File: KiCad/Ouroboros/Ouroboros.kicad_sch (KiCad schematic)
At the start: 0 parts

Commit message: Updating schematic
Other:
- sheet POWER renamed Power
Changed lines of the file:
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@@
 	)
 	(sheet
-		(at 86.36 43.18)
-		(size 12.7 3.81)
+		(at 121.92 34.29)
+		(size 27.94 16.51)
 		(fields_autoplaced yes)
 		(stroke
@@
 			(color 0 0 0 0.0000)
 		)
-		(property "Sheetname" "POWER"
-			(at 86.36 42.4684 0)
+		(property "Sheetname" "Power"
+			(at 121.92 33.5784 0)
 			(effects
 				(font
@@
 		)
 		(property "Sheetfile" "Power.kicad_sch"
-			(at 86.36 47.5746 0)
+			(at 121.92 51.3846 0)
 			(effects
 				(font
@@
 	)
 	(sheet
-		(at 30.48 45.72)
+		(at 29.21 74.93)
 		(size 45.72 36.83)
 		(fields_autoplaced yes)
@@
 		)
 		(property "Sheetname" "Input"
-			(at 30.48 45.0084 0)
+			(at 29.21 74.2184 0)
 			(effects
 				(font
@@
 		)
 		(property "Sheetfile" "input.kicad_sch"
-			(at 30.48 83.1346 0)
+			(at 29.21 112.3446 0)
 			(effects
 				(font
@@
 	)
 	(sheet
-		(at 161.29 53.34)
+		(at 157.48 73.66)
 		(size 64.77 49.53)
 		(fields_autoplaced yes)
@@
 		)
 		(property "Sheetname" "DaisySeed"
-			(at 161.29 52.6284 0)
+			(at 157.48 72.9484 0)
 			(effects
 				(font
@@
 		)
 		(property "Sheetfile" "DaisySeed.kicad_sch"
-			(at 161.29 103.4546 0)
+			(at 157.48 123.7746 0)
 			(effects
 				(font

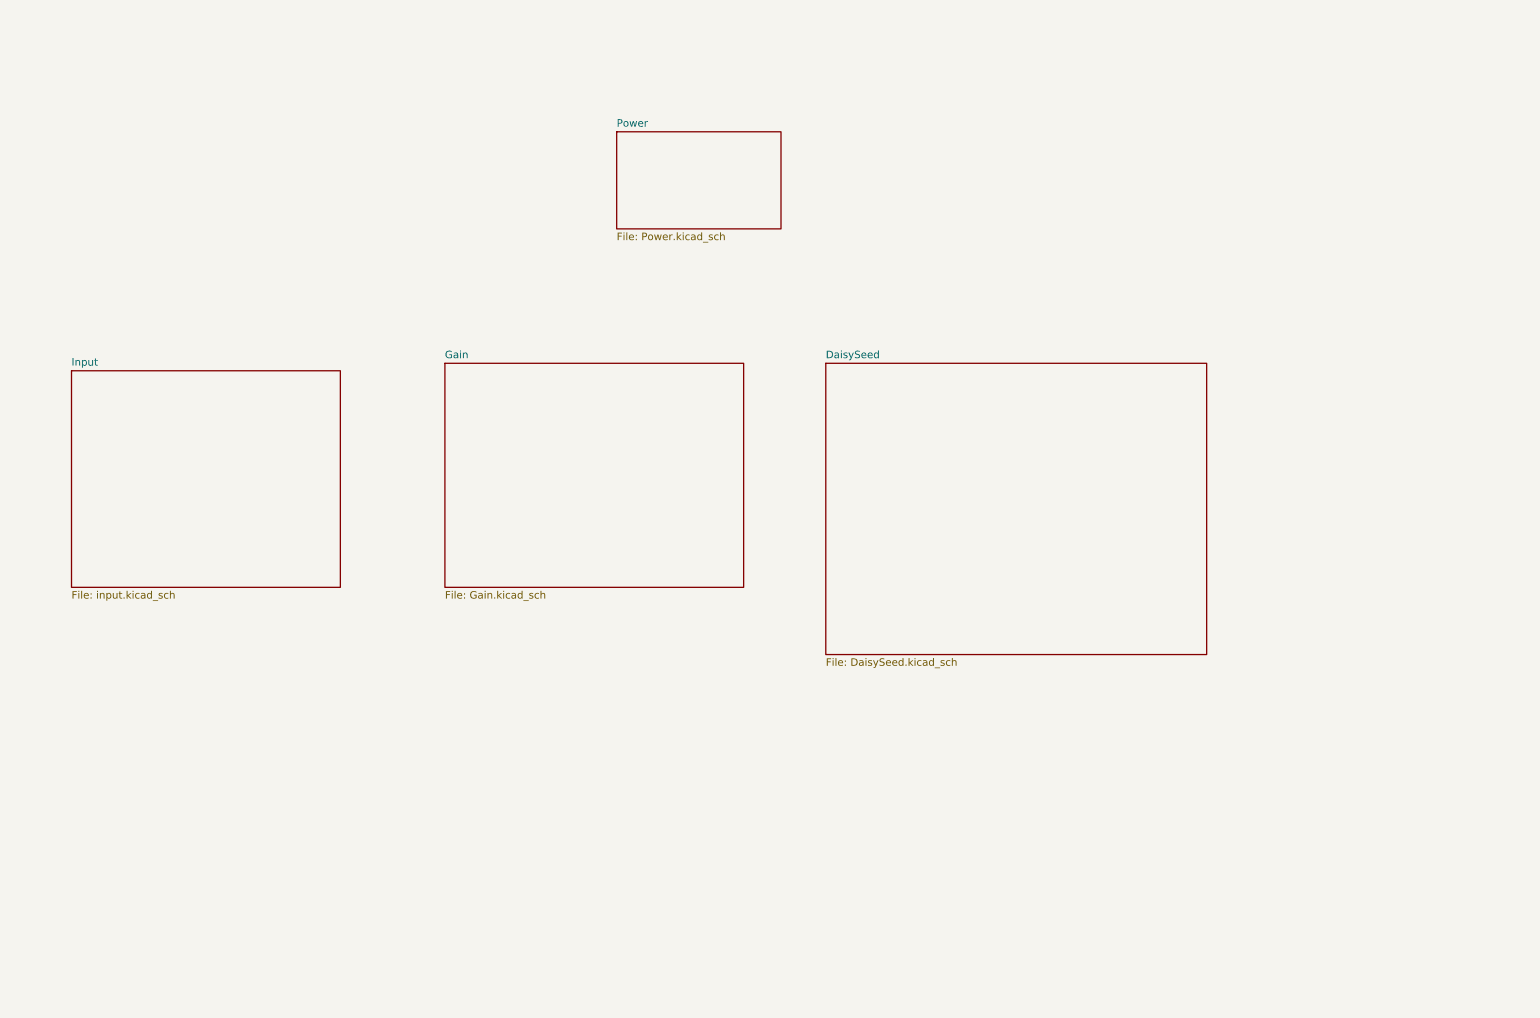
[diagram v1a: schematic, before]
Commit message: Linking nets
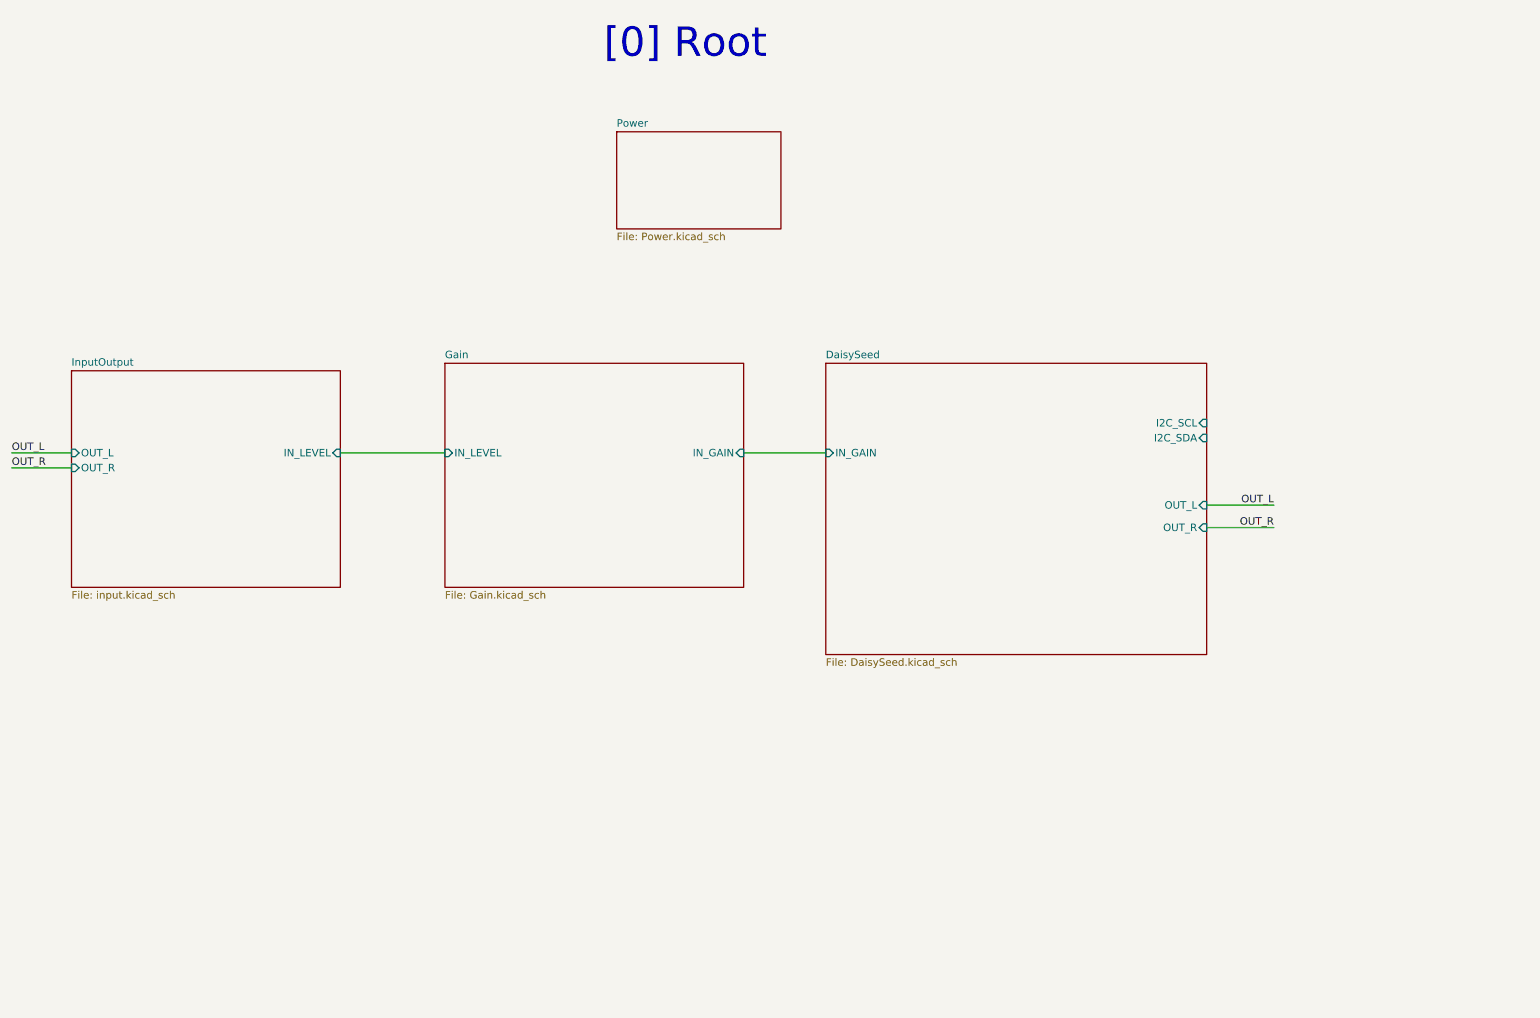
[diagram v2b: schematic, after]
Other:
- sheet Input renamed InputOutput
- sheet DaisySeed ports: added I2C_SCL, I2C_SDA, IN_GAIN, OUT_L, OUT_R; removed none
- sheet Gain ports: added IN_GAIN, IN_LEVEL; removed none
- sheet InputOutput ports: added IN_LEVEL, OUT_L, OUT_R; removed none
- note added: "[0] Root"
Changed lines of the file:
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@@
 	(generator_version "8.0")
 	(paper "A4")
+	(wire
+		(pts
+			(xy 19.05 91.44) (xy 29.21 91.44)
+		)
+		(stroke
+			(width 0)
+			(type default)
+		)
+	)
+	(wire
+		(pts
+			(xy 19.05 88.9) (xy 29.21 88.9)
+		)
+		(stroke
+			(width 0)
+			(type default)
+		)
+	)
+	(wire
+		(pts
+			(xy 74.93 88.9) (xy 92.71 88.9)
+		)
+		(stroke
+			(width 0)
+			(type default)
+		)
+	)
+	(wire
+		(pts
+			(xy 143.51 88.9) (xy 157.48 88.9)
+		)
+		(stroke
+			(width 0)
+			(type default)
+		)
+	)
+	(wire
+		(pts
+			(xy 222.25 101.6) (xy 233.68 101.6)
+		)
+		(stroke
+			(width 0)
+			(type default)
+		)
+	)
+	(wire
+		(pts
+			(xy 222.25 97.79) (xy 233.68 97.79)
+		)
+		(stroke
+			(width 0)
+			(type default)
+		)
+	)
+	(text "[0] Root"
+		(exclude_from_sim no)
+		(at 133.604 19.304 0)
+		(effects
+			(font
+				(size 5 5)
+				(color 132 0 0 1)
+			)
+		)
+	)
+	(label "OUT_L"
+		(at 19.05 88.9 0)
+		(fields_autoplaced yes)
+		(effects
+			(font
+				(size 1.27 1.27)
+			)
+			(justify left bottom)
+		)
+	)
+	(label "OUT_R"
+		(at 19.05 91.44 0)
+		(fields_autoplaced yes)
+		(effects
+			(font
+				(size 1.27 1.27)
+			)
+			(justify left bottom)
+		)
+	)
+	(label "OUT_L"
+		(at 233.68 97.79 180)
+		(fields_autoplaced yes)
+		(effects
+			(font
+				(size 1.27 1.27)
+			)
+			(justify right bottom)
+		)
+	)
+	(label "OUT_R"
+		(at 233.68 101.6 180)
+		(fields_autoplaced yes)
+		(effects
+			(font
+				(size 1.27 1.27)
+			)
+			(justify right bottom)
+		)
+	)
 	(sheet
 		(at 92.71 73.66)
@@
 				)
 				(justify left top)
+			)
+		)
+		(pin "IN_LEVEL" input
+			(at 92.71 88.9 180)
+			(effects
+				(font
+					(size 1.27 1.27)
+				)
+				(justify left)
+			)
+		)
+		(pin "IN_GAIN" input
+			(at 143.51 88.9 0)
+			(effects
+				(font
+					(size 1.27 1.27)
+				)
+				(justify right)
 			)
 		)
@@
 			(color 0 0 0 0.0000)
 		)
-		(property "Sheetname" "Input"
+		(property "Sheetname" "InputOutput"
 			(at 29.21 74.2184 0)
 			(effects
@@
 				)
 				(justify left top)
+			)
+		)
+		(pin "IN_LEVEL" input
+			(at 74.93 88.9 0)
+			(effects
+				(font
+					(size 1.27 1.27)
+				)
+				(justify right)
+			)
+		)
+		(pin "OUT_L" input
+			(at 29.21 88.9 180)
+			(effects
+				(font
+					(size 1.27 1.27)
+				)
+				(justify left)
+			)
+		)
+		(pin "OUT_R" input
+			(at 29.21 91.44 180)
+			(effects
+				(font
+					(size 1.27 1.27)
+				)
+				(justify left)
 			)
 		)
@@
 			)
 		)
+		(pin "I2C_SCL" input
+			(at 222.25 83.82 0)
+			(effects
+				(font
+					(size 1.27 1.27)
+				)
+				(justify right)
+			)
+		)
+		(pin "I2C_SDA" input
+			(at 222.25 86.36 0)
+			(effects
+				(font
+					(size 1.27 1.27)
+				)
+				(justify right)
+			)
+		)
+		(pin "IN_GAIN" input
+			(at 157.48 88.9 180)
+			(effects
+				(font
+					(size 1.27 1.27)
+				)
+				(justify left)
+			)
+		)
+		(pin "OUT_L" input
+			(at 222.25 97.79 0)
+			(effects
+				(font
+					(size 1.27 1.27)
+				)
+				(justify right)
+			)
+		)
+		(pin "OUT_R" input
+			(at 222.25 101.6 0)
+			(effects
+				(font
+					(size 1.27 1.27)
+				)
+				(justify right)
+			)
+		)

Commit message: PCB Finished
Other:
- sheet InputOutput renamed Input
- added sheet OLED (OLED.kicad_sch)
- added sheet Output (output.kicad_sch)
- sheet Input ports: added none; removed OUT_L, OUT_R
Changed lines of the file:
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@@
 	(wire
 		(pts
-			(xy 19.05 91.44) (xy 29.21 91.44)
-		)
-		(stroke
-			(width 0)
-			(type default)
-		)
-	)
-	(wire
-		(pts
-			(xy 19.05 88.9) (xy 29.21 88.9)
+			(xy 82.55 156.21) (xy 92.71 156.21)
 		)
 		(stroke
@@
 	(wire
 		(pts
+			(xy 231.14 78.74) (xy 247.65 78.74)
+		)
+		(stroke
+			(width 0)
+			(type default)
+		)
+	)
+	(wire
+		(pts
 			(xy 143.51 88.9) (xy 157.48 88.9)
 		)
@@
 	(wire
 		(pts
+			(xy 231.14 83.82) (xy 231.14 78.74)
+		)
+		(stroke
+			(width 0)
+			(type default)
+		)
+	)
+	(wire
+		(pts
+			(xy 233.68 82.55) (xy 247.65 82.55)
+		)
+		(stroke
+			(width 0)
+			(type default)
+		)
+	)
+	(wire
+		(pts
+			(xy 82.55 160.02) (xy 92.71 160.02)
+		)
+		(stroke
+			(width 0)
+			(type default)
+		)
+	)
+	(wire
+		(pts
+			(xy 222.25 83.82) (xy 231.14 83.82)
+		)
+		(stroke
+			(width 0)
+			(type default)
+		)
+	)
+	(wire
+		(pts
 			(xy 222.25 101.6) (xy 233.68 101.6)
 		)
@@
 		(pts
 			(xy 222.25 97.79) (xy 233.68 97.79)
+		)
+		(stroke
+			(width 0)
+			(type default)
+		)
+	)
+	(wire
+		(pts
+			(xy 222.25 86.36) (xy 233.68 86.36)
+		)
+		(stroke
+			(width 0)
+			(type default)
+		)
+	)
+	(wire
+		(pts
+			(xy 233.68 86.36) (xy 233.68 82.55)
 		)
 		(stroke
@@
 		)
 	)
+	(label "OUT_R"
+		(at 82.55 160.02 0)
+		(fields_autoplaced yes)
+		(effects
+			(font
+				(size 1.27 1.27)
+			)
+			(justify left bottom)
+		)
+	)
 	(label "OUT_L"
-		(at 19.05 88.9 0)
-		(fields_autoplaced yes)
-		(effects
-			(font
-				(size 1.27 1.27)
-			)
-			(justify left bottom)
-		)
-	)
-	(label "OUT_R"
-		(at 19.05 91.44 0)
+		(at 82.55 156.21 0)
 		(fields_autoplaced yes)
 		(effects
@@
 			)
 			(justify right bottom)
+		)
+	)
+	(sheet
+		(at 247.65 74.93)
+		(size 29.21 19.05)
+		(fields_autoplaced yes)
+		(stroke
+			(width 0.1524)
+			(type solid)
+		)
+		(fill
+			(color 0 0 0 0.0000)
+		)
+		(property "Sheetname" "OLED"
+			(at 247.65 74.2184 0)
+			(effects
+				(font
+					(size 1.27 1.27)
+				)
+				(justify left bottom)
+			)
+		)
+		(property "Sheetfile" "OLED.kicad_sch"
+			(at 247.65 94.5646 0)
+			(effects
+				(font
+					(size 1.27 1.27)
+				)
+				(justify left top)
+			)
+		)
+		(pin "I2C_SCL" input
+			(at 247.65 78.74 180)
+			(effects
+				(font
+					(size 1.27 1.27)
+				)
+				(justify left)
+			)
+		)
+		(pin "I2C_SDA" input
+			(at 247.65 82.55 180)
+			(effects
+				(font
+					(size 1.27 1.27)
+				)
+				(justify left)
+			)
+		)
+		(instances
+			(project "Ouroboros"
+				(path "/a2662f7c-8239-40ad-828c-dd886b1cb258"
+					(page "6")
+				)
+			)
+		)
+	)
+	(sheet
+		(at 92.71 146.05)
+		(size 60.96 34.29)
+		(fields_autoplaced yes)
+		(stroke
+			(width 0.1524)
+			(type solid)
+		)
+		(fill
+			(color 0 0 0 0.0000)
+		)
+		(property "Sheetname" "Output"
+			(at 92.71 145.3384 0)
+			(effects
+				(font
+					(size 1.27 1.27)
+				)
+				(justify left bottom)
+			)
+		)
+		(property "Sheetfile" "output.kicad_sch"
+			(at 92.71 180.9246 0)
+			(effects
+				(font
+					(size 1.27 1.27)
+				)
+				(justify left top)
+			)
+		)
+		(pin "OUT_L" input
+			(at 92.71 156.21 180)
+			(effects
+				(font
+					(size 1.27 1.27)
+				)
+				(justify left)
+			)
+		)
+		(pin "OUT_R" input
+			(at 92.71 160.02 180)
+			(effects
+				(font
+					(size 1.27 1.27)
+				)
+				(justify left)
+			)
+		)
+		(instances
+			(project "Ouroboros"
+				(path "/a2662f7c-8239-40ad-828c-dd886b1cb258"
+					(page "7")
+				)
+			)
 		)
 	)
@@
 			(color 0 0 0 0.0000)
 		)
-		(property "Sheetname" "InputOutput"
+		(property "Sheetname" "Input"
 			(at 29.21 74.2184 0)
 			(effects
@@
 			)
 		)
-		(pin "OUT_L" input
-			(at 29.21 88.9 180)
-			(effects
-				(font
-					(size 1.27 1.27)
-				)
-				(justify left)
-			)
-		)
-		(pin "OUT_R" input
-			(at 29.21 91.44 180)
-			(effects
-				(font
-					(size 1.27 1.27)
-				)
-				(justify left)
-			)
-		)

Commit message: Dev Board complete
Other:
- sheet DaisySeed ports: added IN_L, SEND_SW; removed none
- sheet Input ports: added IN_BUF_R, IN_LEVEL_L; removed IN_LEVEL
- sheet Output ports: added SEND_SW; removed none
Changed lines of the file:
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@@
+	(wire
+		(pts
+			(xy 222.25 106.68) (xy 233.68 106.68)
+		)
+		(stroke
+			(width 0)
+			(type default)
+		)
+	)
 	(wire
 		(pts
@@
 	(wire
 		(pts
+			(xy 83.82 118.11) (xy 157.48 118.11)
+		)
+		(stroke
+			(width 0)
+			(type default)
+		)
+	)
+	(wire
+		(pts
 			(xy 231.14 83.82) (xy 231.14 78.74)
 		)
@@
 	(wire
 		(pts
+			(xy 82.55 165.1) (xy 92.71 165.1)
+		)
+		(stroke
+			(width 0)
+			(type default)
+		)
+	)
+	(wire
+		(pts
 			(xy 233.68 82.55) (xy 247.65 82.55)
 		)
@@
 	(wire
 		(pts
+			(xy 83.82 93.98) (xy 83.82 118.11)
+		)
+		(stroke
+			(width 0)
+			(type default)
+		)
+	)
+	(wire
+		(pts
 			(xy 222.25 101.6) (xy 233.68 101.6)
 		)
@@
 		(pts
 			(xy 222.25 86.36) (xy 233.68 86.36)
+		)
+		(stroke
+			(width 0)
+			(type default)
+		)
+	)
+	(wire
+		(pts
+			(xy 74.93 93.98) (xy 83.82 93.98)
 		)
 		(stroke
@@
 		)
 	)
+	(label "SEND_SW"
+		(at 82.55 165.1 0)
+		(fields_autoplaced yes)
+		(effects
+			(font
+				(size 1.27 1.27)
+			)
+			(justify left bottom)
+		)
+	)
 	(label "OUT_R"
 		(at 233.68 101.6 180)
@@
 			)
 			(justify right bottom)
+		)
+	)
+	(label "SEND_SW"
+		(at 224.79 106.68 0)
+		(fields_autoplaced yes)
+		(effects
+			(font
+				(size 1.27 1.27)
+			)
+			(justify left bottom)
 		)
 	)
@@
 			)
 		)
+		(pin "SEND_SW" input
+			(at 92.71 165.1 180)
+			(effects
+				(font
+					(size 1.27 1.27)
+				)
+				(justify left)
+			)
+		)
 		(instances
 			(project "Ouroboros"
@@
 			)
 		)
-		(pin "IN_LEVEL" input
+		(pin "IN_LEVEL_L" input
 			(at 74.93 88.9 0)
+			(effects
+				(font
+					(size 1.27 1.27)
+				)
+				(justify right)
+			)
+		)
+		(pin "IN_BUF_R" input
+			(at 74.93 93.98 0)
 			(effects
 				(font
@@
 			(effects
 				(font
+					(size 1.27 1.27)
+				)
+				(justify right)
+			)
+		)
+		(pin "IN_L" input
+			(at 157.48 118.11 180)
+			(effects
+				(font
+					(size 1.27 1.27)
+				)
+				(justify left)
+			)
+		)
+		(pin "SEND_SW" input
+			(at 222.25 106.68 0)
+			(effects
+				(font
